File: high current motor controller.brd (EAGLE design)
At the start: 100 x 80 mm, 49 parts, among them IC1 LM2676S, Q1 IPT004N03L, Q2 IPT004N03L, Q3 IPT004N03L, Q4 IPT004N03L

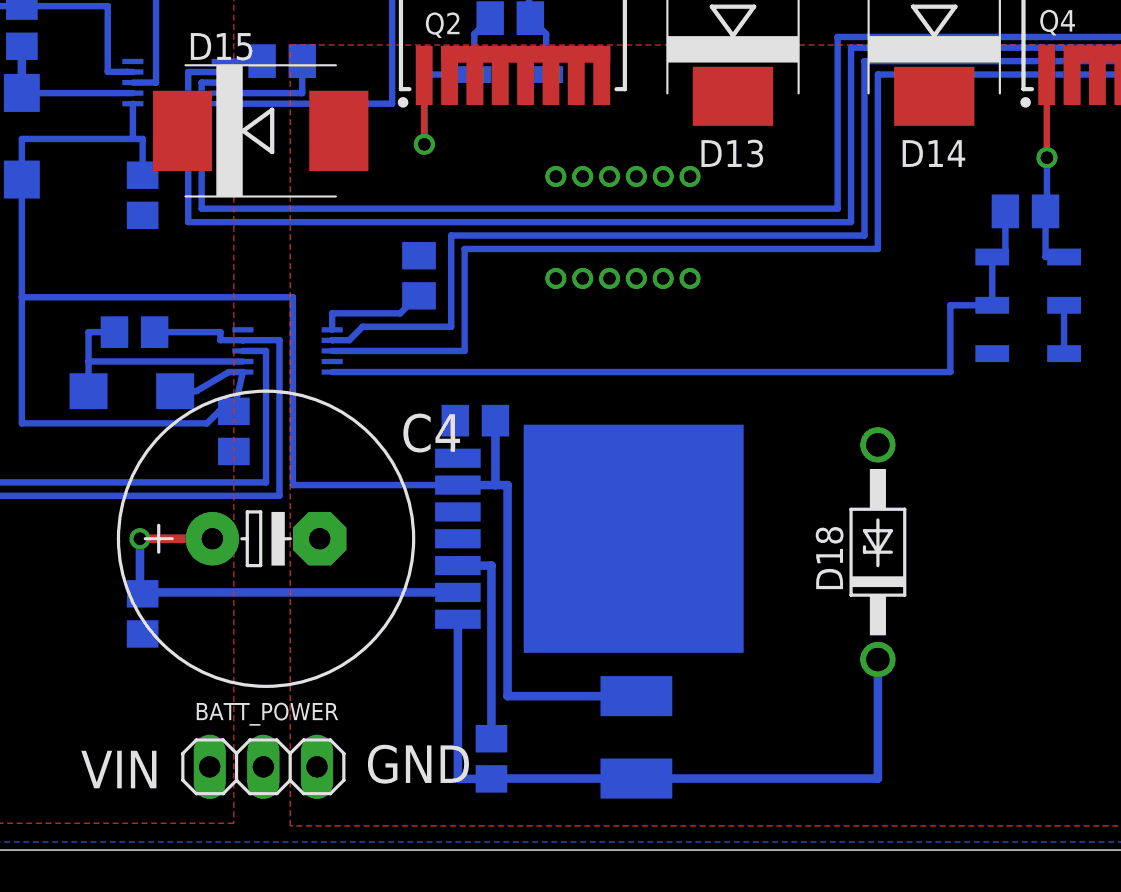
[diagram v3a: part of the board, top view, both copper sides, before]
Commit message: Switching regulator components updated with correct values and packages
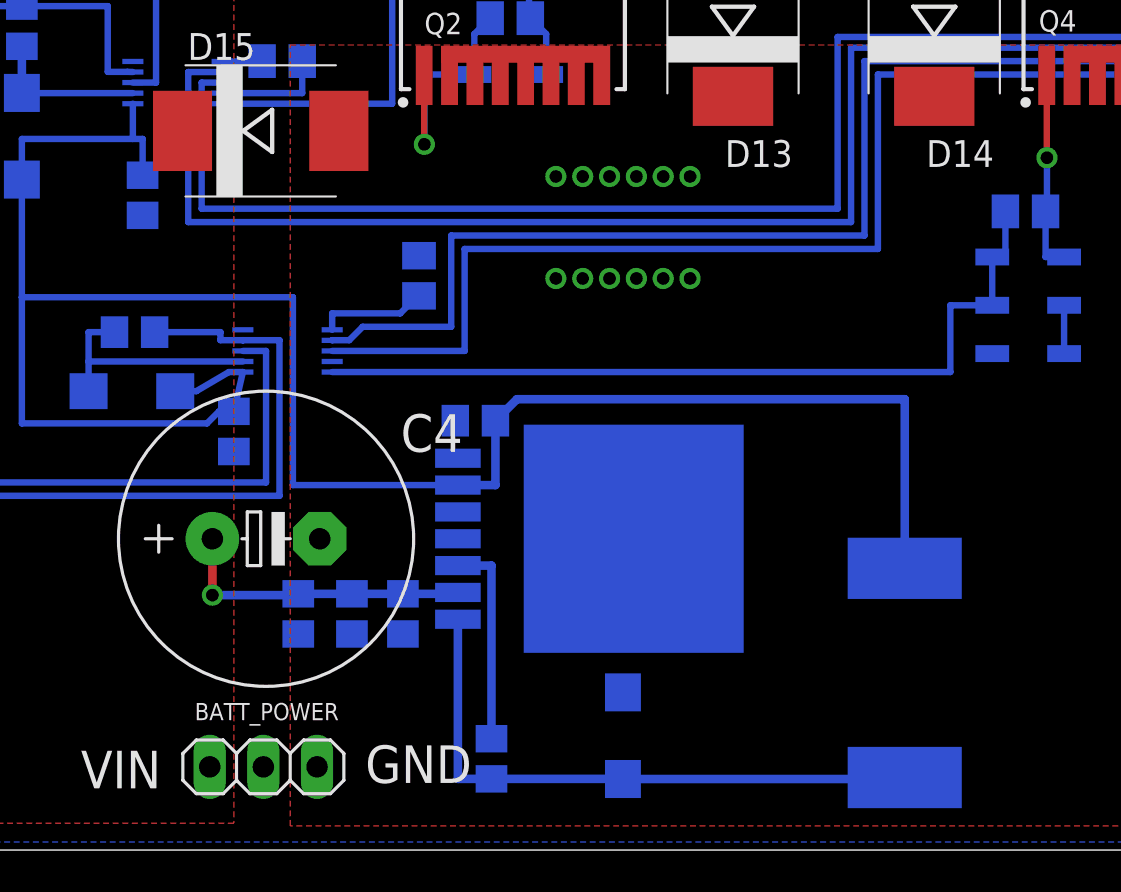
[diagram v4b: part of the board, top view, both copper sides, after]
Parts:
- added C10, C9: 4.7u, resistor:C0805
- C11: value 30u -> 4.7u
- D18: value 1N4728 -> CGRM4001-G; device diode:DO41Z10 -> diode:SMA-DO214AC
- L1: device resistor:L1812 -> resistor:L_WURTH_7447709680
- moved D18 14.9 mm to (67.2, 5.41), flipped to the bottom, turned to 270 degrees
- moved L1 13.1 mm to (80.5, 8.38), turned to 180 degrees
- moved C11 12.3 mm to (56.8, 11.2)
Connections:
- net 12V: now also L1.P$2; no longer L1.2
- net GND: now also C10.2, C9.2
- net N$17: now also D18.K, L1.P$1; no longer D18.C, L1.1
- net VIN: now also C10.1, C9.1
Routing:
- net 12V: track 89.2 -> 100.3 mm
- net VIN: track 21.1 -> 14.4 mm
- net N$17: track 33.1 -> 28.8 mm
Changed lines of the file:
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@@
 <layer number="27" name="tValues" color="7" fill="1" visible="yes" active="yes"/>
 <layer number="28" name="bValues" color="7" fill="1" visible="yes" active="yes"/>
-<layer number="29" name="tStop" color="7" fill="3" visible="no" active="yes"/>
+<layer number="29" name="tStop" color="7" fill="3" visible="yes" active="yes"/>
 <layer number="30" name="bStop" color="7" fill="6" visible="yes" active="yes"/>
-<layer number="31" name="tCream" color="7" fill="4" visible="no" active="yes"/>
-<layer number="32" name="bCream" color="7" fill="5" visible="no" active="yes"/>
-<layer number="33" name="tFinish" color="6" fill="3" visible="no" active="yes"/>
-<layer number="34" name="bFinish" color="6" fill="6" visible="no" active="yes"/>
-<layer number="35" name="tGlue" color="7" fill="4" visible="no" active="yes"/>
-<layer number="36" name="bGlue" color="7" fill="5" visible="no" active="yes"/>
-<layer number="37" name="tTest" color="7" fill="1" visible="no" active="yes"/>
-<layer number="38" name="bTest" color="7" fill="1" visible="no" active="yes"/>
-<layer number="39" name="tKeepout" color="4" fill="11" visible="no" active="yes"/>
+<layer number="31" name="tCream" color="7" fill="4" visible="yes" active="yes"/>
+<layer number="32" name="bCream" color="7" fill="5" visible="yes" active="yes"/>
+<layer number="33" name="tFinish" color="6" fill="3" visible="yes" active="yes"/>
+<layer number="34" name="bFinish" color="6" fill="6" visible="yes" active="yes"/>
+<layer number="35" name="tGlue" color="7" fill="4" visible="yes" active="yes"/>
+<layer number="36" name="bGlue" color="7" fill="5" visible="yes" active="yes"/>
+<layer number="37" name="tTest" color="7" fill="1" visible="yes" active="yes"/>
+<layer number="38" name="bTest" color="7" fill="1" visible="yes" active="yes"/>
+<layer number="39" name="tKeepout" color="4" fill="11" visible="yes" active="yes"/>
 <layer number="40" name="bKeepout" color="1" fill="11" visible="yes" active="yes"/>
-<layer number="41" name="tRestrict" color="4" fill="10" visible="no" active="yes"/>
+<layer number="41" name="tRestrict" color="4" fill="10" visible="yes" active="yes"/>
 <layer number="42" name="bRestrict" color="1" fill="10" visible="yes" active="yes"/>
 <layer number="43" name="vRestrict" color="2" fill="10" visible="no" active="yes"/>
@@
 </element>
 <element name="D13" library="diode" package="SMC" value="" x="72.39" y="39.37" smashed="yes" rot="R90">
-<attribute name="NAME" x="73.944" y="33.598" size="1.27" layer="25" rot="R180"/>
+<attribute name="NAME" x="75.214" y="33.598" size="1.27" layer="25" rot="R180"/>
 <attribute name="VALUE" x="77.019" y="35.911" size="1.27" layer="27" rot="R90"/>
 </element>
 <element name="D14" library="diode" package="SMC" value="" x="81.915" y="39.37" smashed="yes" rot="R90">
-<attribute name="NAME" x="83.469" y="33.598" size="1.27" layer="25" rot="R180"/>
+<attribute name="NAME" x="84.739" y="33.598" size="1.27" layer="25" rot="R180"/>
 <attribute name="VALUE" x="86.544" y="35.911" size="1.27" layer="27" rot="R90"/>
 </element>
@@
 <attribute name="VALUE" x="69.215" y="20.701" size="0.8128" layer="28" rot="MR0"/>
 </element>
-<element name="C11" library="resistor" package="C0805" value="30u" x="44.45" y="11.176" smashed="yes" rot="MR270">
-<attribute name="NAME" x="42.926" y="12.446" size="1.27" layer="26" rot="MR270"/>
+<element name="C11" library="resistor" package="C0805" value="4.7u" x="56.769" y="11.176" smashed="yes" rot="MR270">
+<attribute name="NAME" x="57.277" y="8.636" size="1.016" layer="26" rot="MR270"/>
 </element>
 <element name="C12" library="resistor" package="C0805" value="100u" x="60.198" y="20.32" smashed="yes" rot="MR0">
@@
 <attribute name="NAME" x="62.484" y="6.096" size="1.27" layer="26" rot="MR180"/>
 </element>
-<element name="L1" library="resistor" package="L1812" value="68u" x="67.818" y="5.334" smashed="yes" rot="MR90">
-<attribute name="NAME" x="70.231" y="8.001" size="1.27" layer="26" rot="MR180"/>
-</element>
-<element name="D18" library="diode" package="DO41Z10" value="1N4728" x="79.248" y="14.097" rot="R90"/>
+<element name="L1" library="resistor" package="L_WURTH_7447709680" value="68u" x="80.518" y="8.382" smashed="yes" rot="MR180">
+<attribute name="NAME" x="82.677" y="8.89" size="1.27" layer="26" rot="MR180"/>
+</element>
+<element name="D18" library="diode" package="SMA-DO214AC" value="CGRM4001-G" x="67.182" y="5.412" smashed="yes" rot="MR270">
+<attribute name="NAME" x="68.929015625" y="7.60595625" size="1.27" layer="26" rot="MR180"/>
+</element>
+<element name="C9" library="resistor" package="C0805" value="4.7u" x="51.816" y="11.176" smashed="yes" rot="MR270">
+<attribute name="NAME" x="52.197" y="8.636" size="1.016" layer="26" rot="MR270"/>
+</element>
+<element name="C10" library="resistor" package="C0805" value="4.7u" x="54.356" y="11.176" smashed="yes" rot="MR270">
+<attribute name="NAME" x="54.864" y="8.636" size="1.016" layer="26" rot="MR270"/>
+</element>
 </elements>
 <signals>
@@
 <contactref element="C12" pad="2"/>
 <contactref element="D18" pad="A"/>
-<wire x1="88.44" y1="36.66" x2="81.915" y2="35.67" width="0" layer="19" extent="1-1"/>
+<contactref element="C9" pad="2"/>
+<contactref element="C10" pad="2"/>
 </signal>
 <signal name="12V">
@@
 <wire x1="44.45" y1="31.938" x2="44.45" y2="33.655" width="0.3048" layer="16"/>
 <wire x1="44.45" y1="33.655" x2="43.9879" y2="33.655" width="0.3048" layer="16"/>
-<contactref element="L1" pad="2"/>
+<contactref element="L1" pad="P$2"/>
 <contactref element="C12" pad="1"/>
 <contactref element="IC1" pad="6"/>
-<wire x1="59.371" y1="17.272" x2="61.148" y2="17.272" width="0.4064" layer="16"/>
-<wire x1="61.148" y1="17.272" x2="61.148" y2="20.32" width="0.4064" layer="16"/>
 <wire x1="48.768" y1="20.762" x2="48.067" y2="20.762" width="0.3048" layer="16"/>
 <wire x1="48.067" y1="20.762" x2="47.498" y2="20.193" width="0.3048" layer="16"/>
@@
 <wire x1="51.562" y1="17.272" x2="51.562" y2="26.162" width="0.3048" layer="16"/>
 <wire x1="51.562" y1="26.162" x2="38.735" y2="26.162" width="0.3048" layer="16"/>
-<wire x1="67.818" y1="7.284" x2="61.722" y2="7.284" width="0.4064" layer="16"/>
-<wire x1="61.722" y1="7.284" x2="61.722" y2="17.272" width="0.4064" layer="16"/>
-<wire x1="61.722" y1="17.272" x2="61.148" y2="17.272" width="0.4064" layer="16"/>
+<wire x1="80.518" y1="13.332" x2="80.518" y2="21.336" width="0.4064" layer="16"/>
+<wire x1="80.518" y1="21.336" x2="62.164" y2="21.336" width="0.4064" layer="16"/>
+<wire x1="62.164" y1="21.336" x2="61.148" y2="20.32" width="0.4064" layer="16"/>
+<wire x1="61.148" y1="20.32" x2="61.148" y2="17.272" width="0.4064" layer="16"/>
+<wire x1="61.148" y1="17.272" x2="59.371" y2="17.272" width="0.4064" layer="16"/>
 </signal>
 <signal name="N$3">
@@
 <contactref element="IC1" pad="2"/>
 <contactref element="C11" pad="1"/>
-<wire x1="59.371" y1="12.192" x2="44.45" y2="12.192" width="0.4064" layer="16"/>
-<wire x1="44.45" y1="12.192" x2="44.45" y2="12.126" width="0.4064" layer="16"/>
-<wire x1="44.45" y1="12.126" x2="44.323" y2="12.126" width="0.4064" layer="16"/>
-<wire x1="44.323" y1="12.126" x2="44.323" y2="14.732" width="0.4064" layer="16"/>
-<via x="44.323" y="14.732" extent="1-16" drill="0.6"/>
-<wire x1="44.323" y1="14.732" x2="47.752" y2="14.732" width="0.4064" layer="1"/>
+<contactref element="C10" pad="1"/>
+<contactref element="C9" pad="1"/>
+<wire x1="59.371" y1="12.192" x2="59.371" y2="12.126" width="0.4064" layer="16"/>
+<wire x1="59.371" y1="12.126" x2="56.769" y2="12.126" width="0.4064" layer="16"/>
+<wire x1="56.769" y1="12.126" x2="54.356" y2="12.126" width="0.4064" layer="16"/>
+<wire x1="54.356" y1="12.126" x2="51.816" y2="12.126" width="0.4064" layer="16"/>
+<wire x1="51.816" y1="12.126" x2="51.816" y2="12.065" width="0.4064" layer="16"/>
+<wire x1="51.816" y1="12.065" x2="47.752" y2="12.065" width="0.4064" layer="16"/>
+<via x="47.752" y="12.065" extent="1-16" drill="0.6"/>
+<wire x1="47.752" y1="12.065" x2="47.752" y2="14.732" width="0.4064" layer="1"/>
 </signal>
 <signal name="N$16">
@@
 <signal name="N$17">
 <contactref element="IC1" pad="1"/>
-<contactref element="L1" pad="1"/>
-<contactref element="D18" pad="C"/>
+<contactref element="L1" pad="P$1"/>
+<contactref element="D18" pad="K"/>
 <contactref element="C13" pad="2"/>
 <wire x1="59.371" y1="10.922" x2="59.371" y2="3.368" width="0.4064" layer="16"/>
 <wire x1="59.371" y1="3.368" x2="60.96" y2="3.368" width="0.4064" layer="16"/>
-<wire x1="60.96" y1="3.368" x2="60.96" y2="3.384" width="0.4064" layer="16"/>
-<wire x1="60.96" y1="3.384" x2="67.818" y2="3.384" width="0.4064" layer="16"/>
-<wire x1="67.818" y1="3.384" x2="79.248" y2="3.384" width="0.4064" layer="16"/>
-<wire x1="79.248" y1="3.384" x2="79.248" y2="9.017" width="0.4064" layer="16"/>
+<wire x1="60.96" y1="3.368" x2="67.182" y2="3.368" width="0.4064" layer="16"/>
+<wire x1="67.182" y1="3.368" x2="67.182" y2="3.362" width="0.4064" layer="16"/>
+<wire x1="67.182" y1="3.362" x2="80.518" y2="3.362" width="0.4064" layer="16"/>
+<wire x1="80.518" y1="3.362" x2="80.518" y2="3.432" width="0.4064" layer="16"/>
 </signal>
 </signals>
